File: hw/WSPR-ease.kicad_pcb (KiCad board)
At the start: 4 copper layers, 99 x 64 mm, 132 parts, among them J101 pwr+data, J102 SMA, J103 SMA, K201 G6K-2, K202 G6K-2, K203 G6K-2, Q101 IRLML2060, Q201 IRLML2060, Q202 IRLML2060, Q203 IRLML2060, Q301 IRLML2060, Q302 IRLML2060, Q303 IRLML2060, Q304 IRLML2060, T301 BN-43-202_DualPri_CTSec, U101 SRV05-4, U102 ESP32-S3-WROOM-1-N8R8, U103 LMR51430YDDCR, U104 GNSS module, U301 LCMXO2-256HC-4SG32C, U302 UCC27523DGN, U303 UCC27523DGN, U304 SI5351A-B-GT, Y301 20MHz

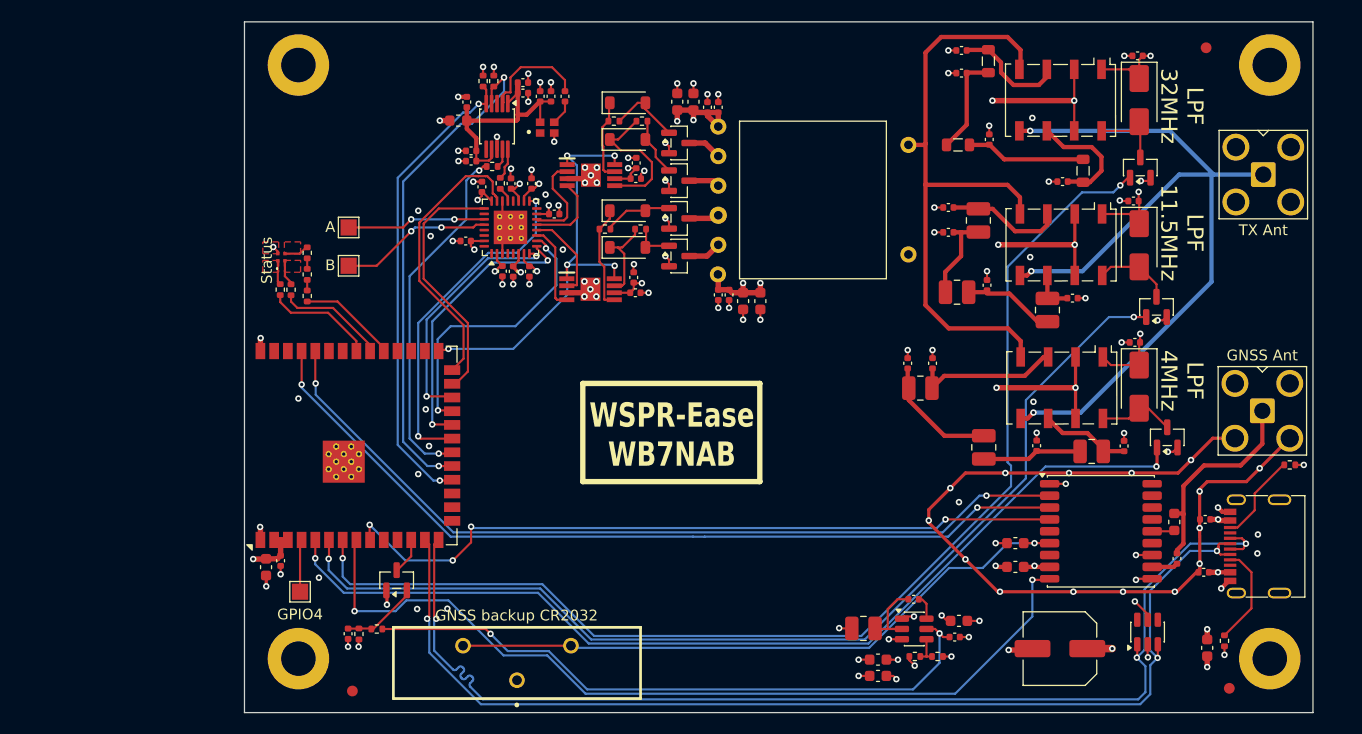
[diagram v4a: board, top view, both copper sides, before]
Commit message: Add stitched GND zone around edge of PCB on all layers and pretty up the mounting holes with vias as well.
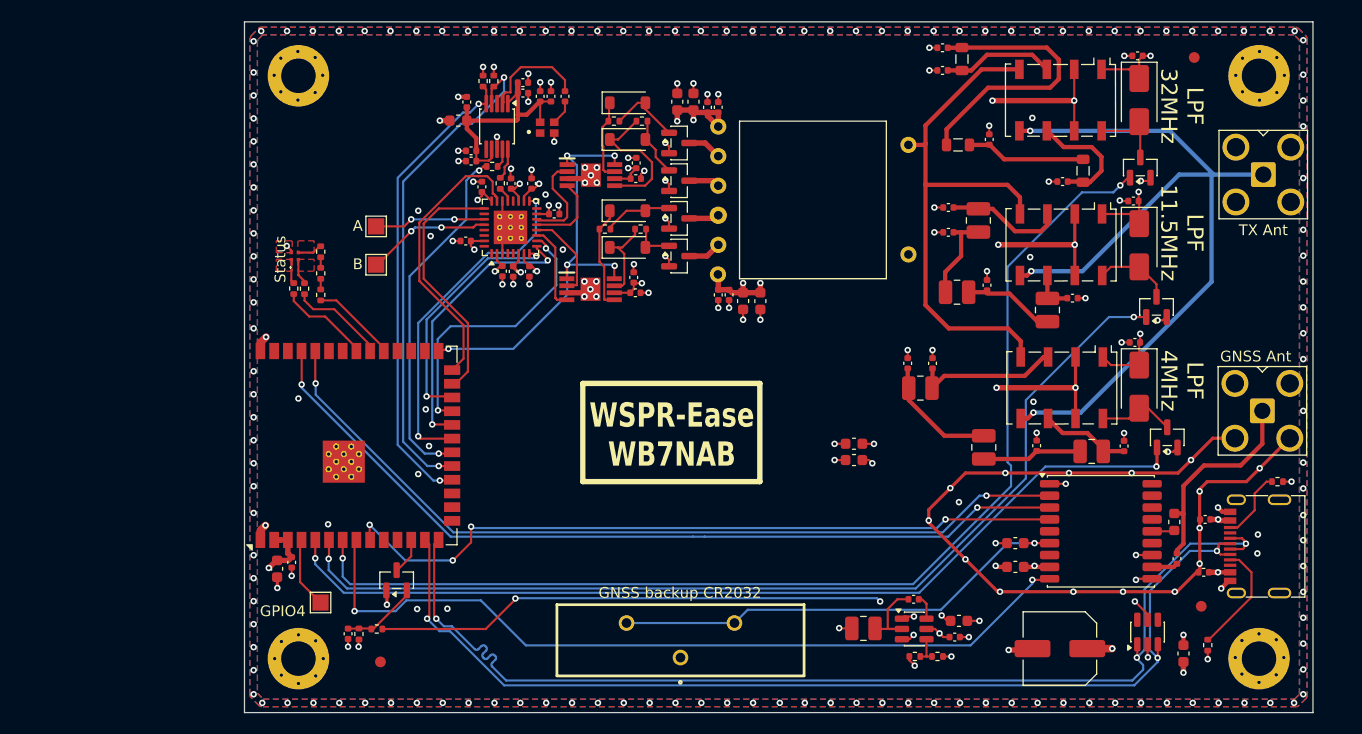
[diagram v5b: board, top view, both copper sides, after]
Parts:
- moved C115 20.1 mm to (106.1, 108.5)
- moved C114 20.1 mm to (106.1, 110.0)
- moved BT101 15.3 mm to (90.0, 126.7)
- moved FID101 8.03 mm to (138.2, 123.5)
- moved FID103 3.75 mm to (62.2, 128.7)
- moved C213 2.93 mm to (114.3, 71.8)
- moved TP301 2.55 mm to (61.8, 88.3)
- moved TP302 2.55 mm to (61.8, 91.9)
- moved C212 2.55 mm to (114.3, 73.9)
- moved L207 2.46 mm to (116.1, 72.8), turned to 90 degrees
- moved C103 2.26 mm to (136.6, 127.9)
- moved TP101 2.15 mm to (56.6, 123.2)
- moved R102 1.92 mm to (145.3, 112.0)
- moved R101 1.60 mm to (138.8, 127.2)
- moved FID102 1.42 mm to (137.6, 72.7)
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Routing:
- net Net-(C213-Pad1): track 9.08 -> 26.3 mm
- net Net-(U104-V_BCKP): track 59.4 -> 43.5 mm
- net VBUS: track 111.2 -> 101.4 mm, vias 17 -> 18
- net /Low Pass Filters/RFin: track 59.1 -> 51.6 mm
- net /gnssNRESET: track 81.1 -> 75.6 mm
- net /D-: track 102.6 -> 98.0 mm
- net /D+: track 106.8 -> 102.3 mm
- net /hiON: track 108.5 -> 104.5 mm
- net /midON: track 97.8 -> 93.9 mm
- net /loON: track 91.8 -> 87.9 mm
- net Net-(U301A-SCL/PCLKT0_0): track 14.1 -> 11.4 mm
- net Net-(U301A-SDA/PCLKC0_0): track 12.9 -> 10.3 mm
- net /hbBlu: track 10.1 -> 8.25 mm
- net Net-(U102-IO4): track 4.66 -> 6.45 mm
- net Net-(J101-CC2): track 8.24 -> 6.55 mm
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- added copper zone on B.Cu, net GND
- added copper zone on F.Cu, net GND
- added copper zone on In2.Cu, net GND

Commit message: Prep to go back to FPGA. Board is routed except for power layer zones. No time to run DRC yet.
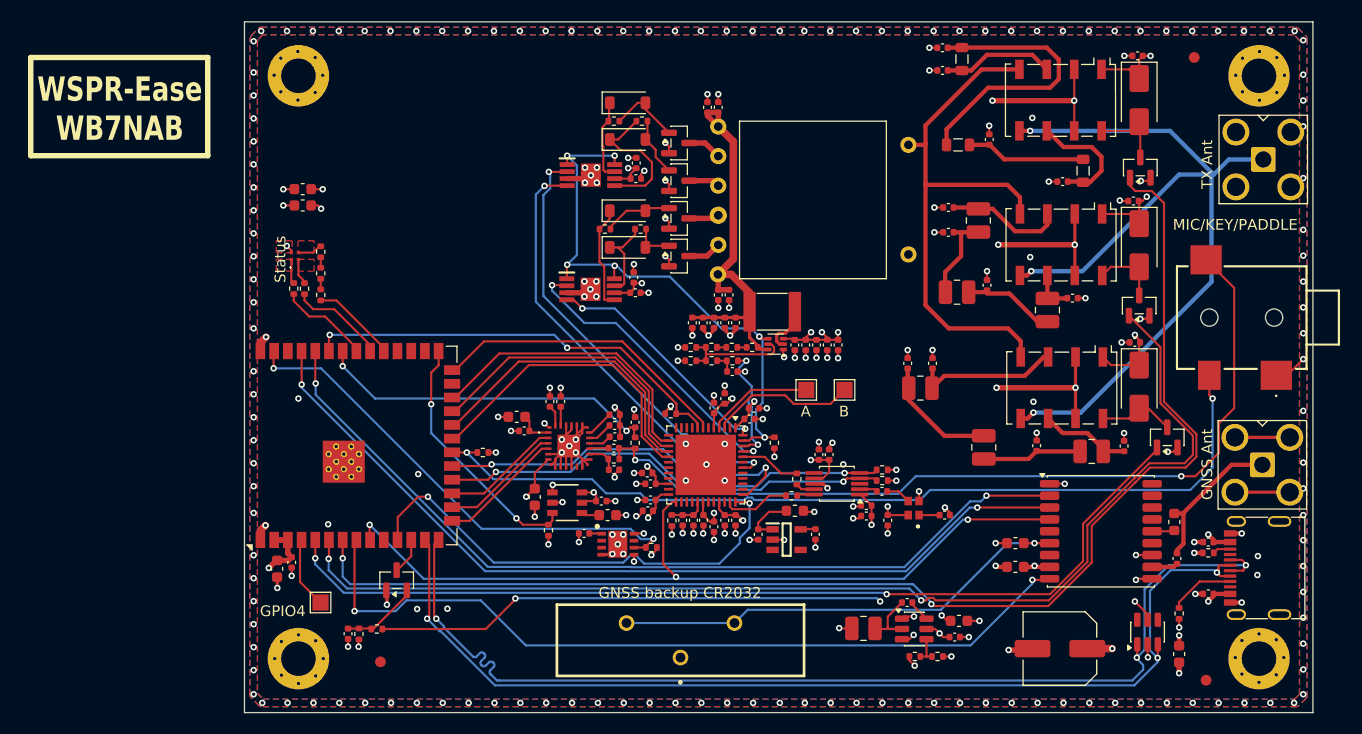
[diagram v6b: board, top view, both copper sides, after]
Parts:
- removed the C301 at (76.2, 84.4)
- removed the C302 at (70.1, 89.7)
- removed the C303 at (73.5, 92.5)
- removed the C304 at (71.6, 84.7)
- removed the C305 at (89.7, 76.8)
- removed the C307 at (91.2, 76.8)
- removed C319, C327: 1uF X5R 25V, Capacitor_SMD:C_0402_1005Metric
- removed C322, C325, C326, C328: 100nF X7R 50V, Capacitor_SMD:C_0402_1005Metric
- removed FB301: 600@1A, Inductor_SMD:L_0603_1608Metric
- removed the U301 at (74.2, 88.4)
- removed Y301: 20MHz, Library:ECSTXO201633400TR
- added C106: 1uF, Capacitor_SMD:C_0402_1005Metric, F.Cu at (81.1, 116.8)
- added C108: 1uF, Capacitor_SMD:C_0402_1005Metric, F.Cu at (82.7, 113.8)
- added C109: 1nF NP0 100V, Capacitor_SMD:C_0603_1608Metric, F.Cu at (83.2, 115.1)
- added C119: 1uF X5R 25V, Capacitor_SMD:C_0402_1005Metric, F.Cu at (97.2, 116.9)
- added C120: 1uF X5R 25V, Capacitor_SMD:C_0402_1005Metric, F.Cu at (102.5, 116.9)
- added C309: 1uF X5R 25V, Capacitor_SMD:C_0402_1005Metric, F.Cu at (104.6, 99.3)
- added C310: 1uF X5R 25V, Capacitor_SMD:C_0402_1005Metric, F.Cu at (103.6, 99.3)
- added C313: 1uF X5R 25V, Capacitor_SMD:C_0402_1005Metric, F.Cu at (100.6, 99.3)
- added C314: 1uF X5R 25V, Capacitor_SMD:C_0402_1005Metric, F.Cu at (95.1, 97.3)
- added C315: 1uF X5R 25V, Capacitor_SMD:C_0402_1005Metric, F.Cu at (94.1, 97.3)
- added C317: 1uF X5R 25V, Capacitor_SMD:C_0402_1005Metric, F.Cu at (92.1, 97.3)
- added C401: 100nF X7R 50V, Capacitor_SMD:C_0402_1005Metric, F.Cu at (94.1, 115.6)
- added C402: 100nF X7R 50V, Capacitor_SMD:C_0402_1005Metric, F.Cu at (92.1, 115.6)
- added C403: 100nF X7R 50V, Capacitor_SMD:C_0402_1005Metric, F.Cu at (93.1, 105.2)
- added C404: 4.7uF, Capacitor_SMD:C_0402_1005Metric, F.Cu at (95.1, 115.6)
- added C405: 100nF X7R 50V, Capacitor_SMD:C_0402_1005Metric, F.Cu at (75.5, 107.3)
- added C406: 10uF X5R 25V, Capacitor_SMD:C_0603_1608Metric, F.Cu at (74.8, 106.0)
- added C407: 4.7uF, Capacitor_SMD:C_0402_1005Metric, F.Cu at (93.1, 116.2)
- added C408: 4.7uF, Capacitor_SMD:C_0402_1005Metric, F.Cu at (94.1, 104.3)
- added C409: 10uF X5R 25V, Capacitor_SMD:C_0603_1608Metric, F.Cu at (76.5, 113.4)
- added C410: 1uF X5R 25V, Capacitor_SMD:C_0402_1005Metric, F.Cu at (78.9, 104.6)
- added C411: 1uF X5R 25V, Capacitor_SMD:C_0402_1005Metric, F.Cu at (83.8, 110.9)
- added C412: 100nF X7R 50V, Capacitor_SMD:C_0402_1005Metric, F.Cu at (87.2, 113.7)
- added C413: 4.7uF, Capacitor_SMD:C_0402_1005Metric, F.Cu at (90.2, 115.6)
- added C414: 100nF X7R 50V, Capacitor_SMD:C_0402_1005Metric, F.Cu at (91.2, 115.6)
- added C415: 4.7uF, Capacitor_SMD:C_0402_1005Metric, F.Cu at (87.0, 114.7)
- added C416: 1uF X5R 25V, Capacitor_SMD:C_0402_1005Metric, F.Cu at (83.8, 108.9)
- added C417: 1uF X5R 25V, Capacitor_SMD:C_0402_1005Metric, F.Cu at (83.9, 107.8)
- added C418: 1uF X5R 25V, Capacitor_SMD:C_0402_1005Metric, F.Cu at (83.9, 106.8)
- added C419: 1uF X5R 25V, Capacitor_SMD:C_0402_1005Metric, F.Cu at (83.9, 105.8)
- added C420: 1uF X5R 25V, Capacitor_SMD:C_0402_1005Metric, F.Cu at (77.9, 104.6)
- added C421: 100nF X7R 50V, Capacitor_SMD:C_0402_1005Metric, F.Cu at (87.2, 112.2)
- added C422: 4.7uF, Capacitor_SMD:C_0402_1005Metric, F.Cu at (86.9, 111.2)
- added C423: 1.6nF NP0 25V, Capacitor_SMD:C_0402_1005Metric, F.Cu at (94.8, 101.8)
- added C424: 330pF NP0 50V, Capacitor_SMD:C_0402_1005Metric, F.Cu at (85.8, 106.5)
- added C425: 100nF X7R 50V, Capacitor_SMD:C_0402_1005Metric, F.Cu at (96.4, 106.2)
- added C426: 4.7uF, Capacitor_SMD:C_0402_1005Metric, F.Cu at (96.8, 105.2)
- added C431: 100nF X7R 50V, Capacitor_SMD:C_0402_1005Metric, F.Cu at (108.7, 112.9)
- added C432: 1uF, Capacitor_SMD:C_0402_1005Metric, F.Cu at (114.5, 115.1)
- added C433: 100nF X7R 50V, Capacitor_SMD:C_0402_1005Metric, F.Cu at (109.2, 115.6)
- added FB101: 600@1A, Inductor_SMD:L_0603_1608Metric, F.Cu at (100.6, 114.7)
- added J402: SJ1-3514-SMT-TR, Library:35RASMT2BHWNTRX, F.Cu at (142.0, 96.8)
- added L301: 1uH@2A, Library:PFL4514-inductor, F.Cu at (98.5, 96.3)
- added R101: 10k, Resistor_SMD:R_0402_1005Metric, F.Cu at (87.3, 118.1)
- added R105: 10k, Resistor_SMD:R_0402_1005Metric, F.Cu at (77.8, 116.5)
- added R305: 5.1k, Resistor_SMD:R_0402_1005Metric, F.Cu at (96.6, 99.6)
- added R306: 5.1k, Resistor_SMD:R_0402_1005Metric, F.Cu at (94.8, 99.6)
- added R307: 5.1k, Resistor_SMD:R_0402_1005Metric, F.Cu at (92.9, 99.6)
- added R308: 5.1k, Resistor_SMD:R_0402_1005Metric, F.Cu at (92.9, 100.8)
- added R309: 5.1k, Resistor_SMD:R_0402_1005Metric, F.Cu at (90.9, 99.6)
- added R310: 5.1k, Resistor_SMD:R_0402_1005Metric, F.Cu at (90.9, 100.8)
- added R401: 100, Resistor_SMD:R_0402_1005Metric, F.Cu at (89.2, 115.6)
- added R402: 5.1k, Resistor_SMD:R_0402_1005Metric, F.Cu at (83.8, 109.9)
- added R403: 5.1k, Resistor_SMD:R_0402_1005Metric, F.Cu at (94.8, 100.8)
- added R404: 10k, Resistor_SMD:R_0402_1005Metric, F.Cu at (71.7, 109.3)
- added R405: 10k, Resistor_SMD:R_0402_1005Metric, F.Cu at (85.8, 108.4)
- added R408: 10k, Resistor_SMD:R_0402_1005Metric, F.Cu at (98.7, 108.4)
- added R409: 10k, Resistor_SMD:R_0402_1005Metric, F.Cu at (89.1, 105.7)
- added U101: TPS74612PQWDRBRQ1, Library:SON65P300X300X100-9N-D, F.Cu at (84.2, 117.8)
- added U103: TPS22918DBVR, Library:DBV6_TEX, F.Cu at (79.5, 113.9)
- added U107: AP2112K-3.3TRG1, Library:SOT95P285X140-5N, F.Cu at (99.8, 117.4)
- added U303: TPS62A02NDRL, Package_TO_SOT_SMD:SOT-563, F.Cu at (98.8, 99.3)
- added U402: ICE40UP5K-SG48ITR, Package_DFN_QFN:QFN-48-1EP_7x7mm_P0.5mm_EP5.6x5.6mm, F.Cu at (92.3, 110.5)
- added U403: TAA5242IRGER, Library:TAA5242IRGER, F.Cu at (79.7, 108.7)
- added Y401: 40MHz, Library:ECSTXO201633400TR, F.Cu at (111.6, 114.5)
- C311, C312: value 100nF X7R 50V -> 1uF X5R 25V
- C316, C318: value 10uF X5R 25V -> 1uF X5R 25V; footprint Capacitor_SMD:C_0603_1608Metric -> Capacitor_SMD:C_0402_1005Metric
- moved C117 56.3 mm to (55.0, 86.4)
- moved C118 56.3 mm to (55.0, 84.9)
- moved R410 51.6 mm to (108.7, 111.9), turned to 0 degrees
- moved R411 51.6 mm to (108.7, 110.9), turned to 0 degrees
- moved C427 51.2 mm to (107.2, 115.2), turned to 180 degrees
- moved C429 49.7 mm to (107.2, 114.2), turned to 0 degrees
- moved U404 45.7 mm to (104.5, 112.2), turned to 180 degrees
- moved TP402 44.9 mm to (105.2, 103.5), turned to -90 degrees
- moved C430 42.9 mm to (103.8, 109.5), turned to -90 degrees
- moved C428 42.8 mm to (102.8, 109.5), turned to 90 degrees
- moved TP401 42.6 mm to (101.7, 103.5), turned to -90 degrees
- moved R407 40.4 mm to (100.8, 111.8), turned to -90 degrees
- moved R406 39.6 mm to (100.3, 113.3), turned to 0 degrees
- moved C311 27.2 mm to (102.6, 99.3), turned to -90 degrees
- moved C312 26.5 mm to (101.6, 99.3), turned to -90 degrees
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- renumbered C106 to C107, C107 to C110, C108 to C111, C109 to C112, C110 to C113, C111 to C114, C112 to C115, C113 to C116, C114 to C117, C115 to C118, C306 to C301, C308 to C302, C309 to C303, C310 to C304, C313 to C305, C315 to C306, C314 to C307, C317 to C308, C320 to C427, C321 to C428, C323 to C429, C324 to C430, R101 to R102, R102 to R103, R103 to R104, R104 to R106, R105 to R107, R106 to R108, R107 to R109, R108 to R110, R109 to R111, R110 to R112, R111 to R113, R305 to R406, R306 to R407, R307 to R410, R308 to R411, TP301 to TP401, TP302 to TP402, U101 to U102, U102 to U104, U103 to U105, U104 to U106, U302 to U301, U303 to U302, U304 to U404
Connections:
- C302 pad 1: VBUS -> VPA
- C304 pad 1: VBUS -> VPA
- C305 pad 1: VBUS -> VPA
- C307 pad 1: VBUS -> VPA
- C311 pad 1: GND -> VBUS
- C311 pad 2: +3.3V -> GND
- C312 pad 1: GND -> VBUS
- C312 pad 2: +3.3V -> GND
- C316 pad 1: VBUS -> VPA
- C318 pad 1: VBUS -> VPA
- R406 pad 1: Net-(U301B-PCLKT1_0) -> /Exciter/FPGACLK
- R407 pad 1: /tcxo -> /Exciter/txco
- R410 pad 1: /txSCL -> /txSDA
- R411 pad 1: /txSDA -> /txSCL
- T301 pad 1: VBUS -> VPA
- T301 pad 6: VBUS -> VPA
- U104 pad 11: unconnected-(U102-IO18-Pad11) -> /fpgaNRESET
- U104 pad 15: unconnected-(U102-IO3-Pad15) -> /micDOUT
- U104 pad 16: unconnected-(U102-IO46-Pad16) -> /txSYNC
- U104 pad 17: unconnected-(U102-IO9-Pad17) -> /txBCLK
- U104 pad 20: /tcxo -> /keyerDahPTT
- U104 pad 21: /cpldMOSI -> /fpgaMOSI
- U104 pad 22: /cpldSCK -> /fpgaNCS
- U104 pad 23: /cpldMISO -> /fpgaSCK
- U104 pad 24: /cpldNCS -> /fpgaMISO
- U104 pad 25: /cpldPROG -> /fpgaPROG
- U104 pad 26: /cpldDONE -> /fpgaDONE
- U104 pad 27: /paEn -> /enFPGAIO
- U104 pad 34: unconnected-(U102-IO41-Pad34) -> /keyerDit
- U104 pad 35: unconnected-(U102-IO42-Pad35) -> /fpgaCRESET
- U104 pad 39: unconnected-(U102-IO1-Pad39) -> /pgFPGACORE
- U301 pad 2: /Transmitter/nPushBase -> /Exciter/nPushBase
- U301 pad 4: /Transmitter/nPushPeak -> /Exciter/nPushPeak
- U302 pad 2: /Transmitter/nPullBase -> /Exciter/nPullBase
- U302 pad 4: /Transmitter/nPullPeak -> /Exciter/nPullPeak
- U404 pad 4: /txSCL -> /txSDA
- U404 pad 5: /txSDA -> /txSCL
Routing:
- net /keyerDahPTT: track 0.00 -> 83.5 mm, vias 0 -> 2
- net /Exciter/micTip: track 0.00 -> 80.1 mm, vias 0 -> 2
- net /pgFPGACORE: track 0.00 -> 45.6 mm, vias 0 -> 2
- net /Exciter/nPushPeak: track 0.00 -> 45.0 mm, vias 0 -> 2
- net /fpgaNRESET: track 0.00 -> 43.9 mm, vias 0 -> 2
- net /Exciter/nPushBase: track 0.00 -> 40.7 mm, vias 0 -> 2
- net /fpgaCRESET: track 0.00 -> 40.0 mm, vias 0 -> 2
- net VPA: track 0.00 -> 36.8 mm
- net /tcxo: track 32.8 -> 0.00 mm, vias 2 -> 0
- net /keyerDit: track 0.00 -> 32.0 mm, vias 0 -> 2
- net /cpldMOSI: track 31.7 -> 0.00 mm, vias 2 -> 0
- net /fpgaMOSI: track 0.00 -> 28.7 mm
- net /fpgaNCS: track 0.00 -> 28.3 mm
- net /fpgaDONE: track 0.00 -> 28.0 mm
- net /fpgaSCK: track 0.00 -> 27.8 mm
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- added copper zone on In2.Cu, net +VDDA
- added copper zone on In2.Cu, net +VFPGACORE
- added copper zone on In2.Cu, net +VFPGAIO
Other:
- board text removed: "LPF 11.5MHz"
- board text removed: "LPF 32MHz"
- board text removed: "LPF 4MHz"

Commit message: Now we pass schematic and PCB DRC and 3D renders nicely also.
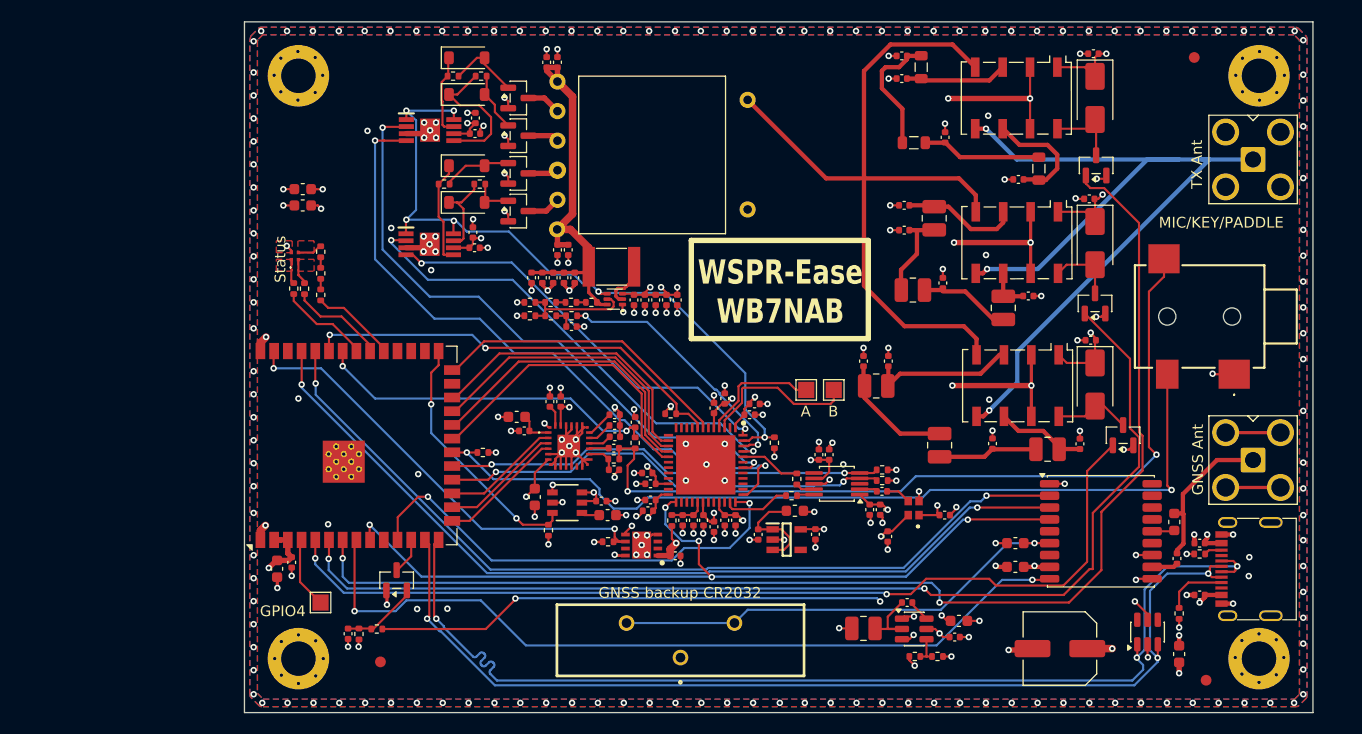
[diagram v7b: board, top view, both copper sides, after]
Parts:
- U401: renamed from U402; footprint Package_DFN_QFN:QFN-48-1EP_7x7mm_P0.5mm_EP5.6x5.6mm -> Library:QFN50P700X700X100-49N-D
- moved C301 15.5 mm to (71.0, 78.3)
- moved C302 15.5 mm to (77.6, 73.1)
- moved C303 15.5 mm to (71.0, 79.8)
- moved C304 15.5 mm to (78.6, 73.1)
- moved C305 15.5 mm to (78.6, 90.5)
- moved C306 15.5 mm to (70.8, 88.9)
- moved C307 15.5 mm to (79.6, 90.5)
- moved C313 15.5 mm to (85.7, 95.2)
- moved L301 15.5 mm to (83.6, 92.1)
- moved Q301 15.5 mm to (75.0, 79.9)
- moved Q302 15.5 mm to (75.0, 76.5)
- moved Q304 15.5 mm to (75.0, 83.4)
- moved R404 15.5 mm to (79.9, 96.6)
- moved U302 15.5 mm to (66.8, 90.0)
- moved U303 15.5 mm to (83.9, 95.1)
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- renumbered J402 to J401, R404 to R403, R403 to R404, U403 to U402, U404 to U403
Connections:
- C119 pad 1: Net-(U107-VIN) -> Net-(U107-EN)
- FB101 pad 2: Net-(U107-VIN) -> Net-(U107-EN)
- U104 pad 25: /fpgaPROG -> unconnected-(U104-IO48-Pad25)
- U107 pad 1: Net-(U107-VIN) -> Net-(U107-EN)
- U107 pad 3: unconnected-(U107-EN-Pad3) -> Net-(U107-EN)
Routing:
- net /Low Pass Filters/RFin: track 51.6 -> 72.1 mm
- net /Exciter/nPushPeak: track 45.0 -> 62.2 mm
- net /Exciter/nPullPeak: track 22.2 -> 38.9 mm
- net /Exciter/nPushBase: track 40.7 -> 57.4 mm
- net /Exciter/nPullBase: track 27.7 -> 44.1 mm
- net Net-(C213-Pad1): track 26.3 -> 11.8 mm
- net /paEn: track 54.0 -> 67.3 mm
- net /Exciter/amPWM: track 11.3 -> 23.9 mm
- net Net-(U107-EN): track 0.00 -> 9.30 mm
- net Net-(U107-VIN): track 4.98 -> 0.00 mm
- net /Low Pass Filters/RFout: track 79.5 -> 83.8 mm
- net /midON: track 107.2 -> 103.1 mm
- net /Exciter/micTip: track 80.1 -> 76.1 mm
- net /pgFPGACORE: track 45.6 -> 42.3 mm
- net /hiON: track 120.9 -> 117.6 mm
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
